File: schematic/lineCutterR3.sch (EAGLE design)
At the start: 63 parts, among them J1 10118192-0001LF, Q1 AO4576, Q2 AO4576, Q4 AO4576, Q5 DMG2305, SW1 KMR2, U1 MS560702BA03-50, U2 MDBT50Q, U3 S25FL128SDPMFIG13S03016, U4 ACS711KEXLT-31AB-T, U6 ICM-20602, X1 2x5 0.05"

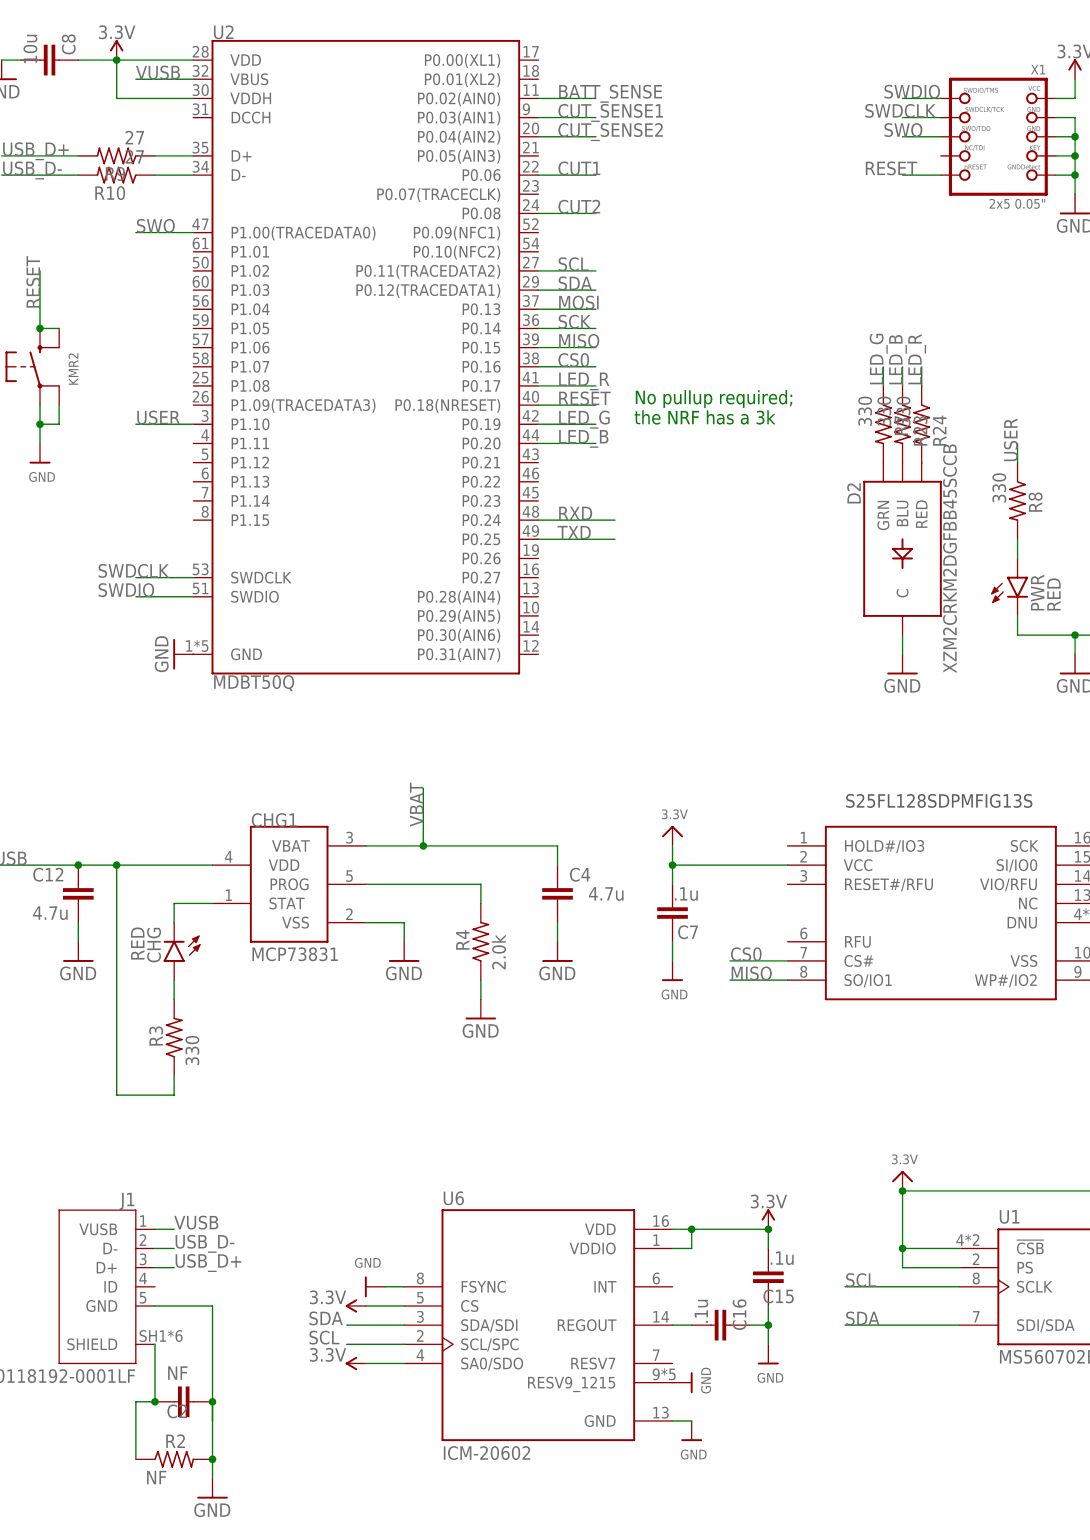
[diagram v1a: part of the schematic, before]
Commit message: R3 PCB: Place most of the components
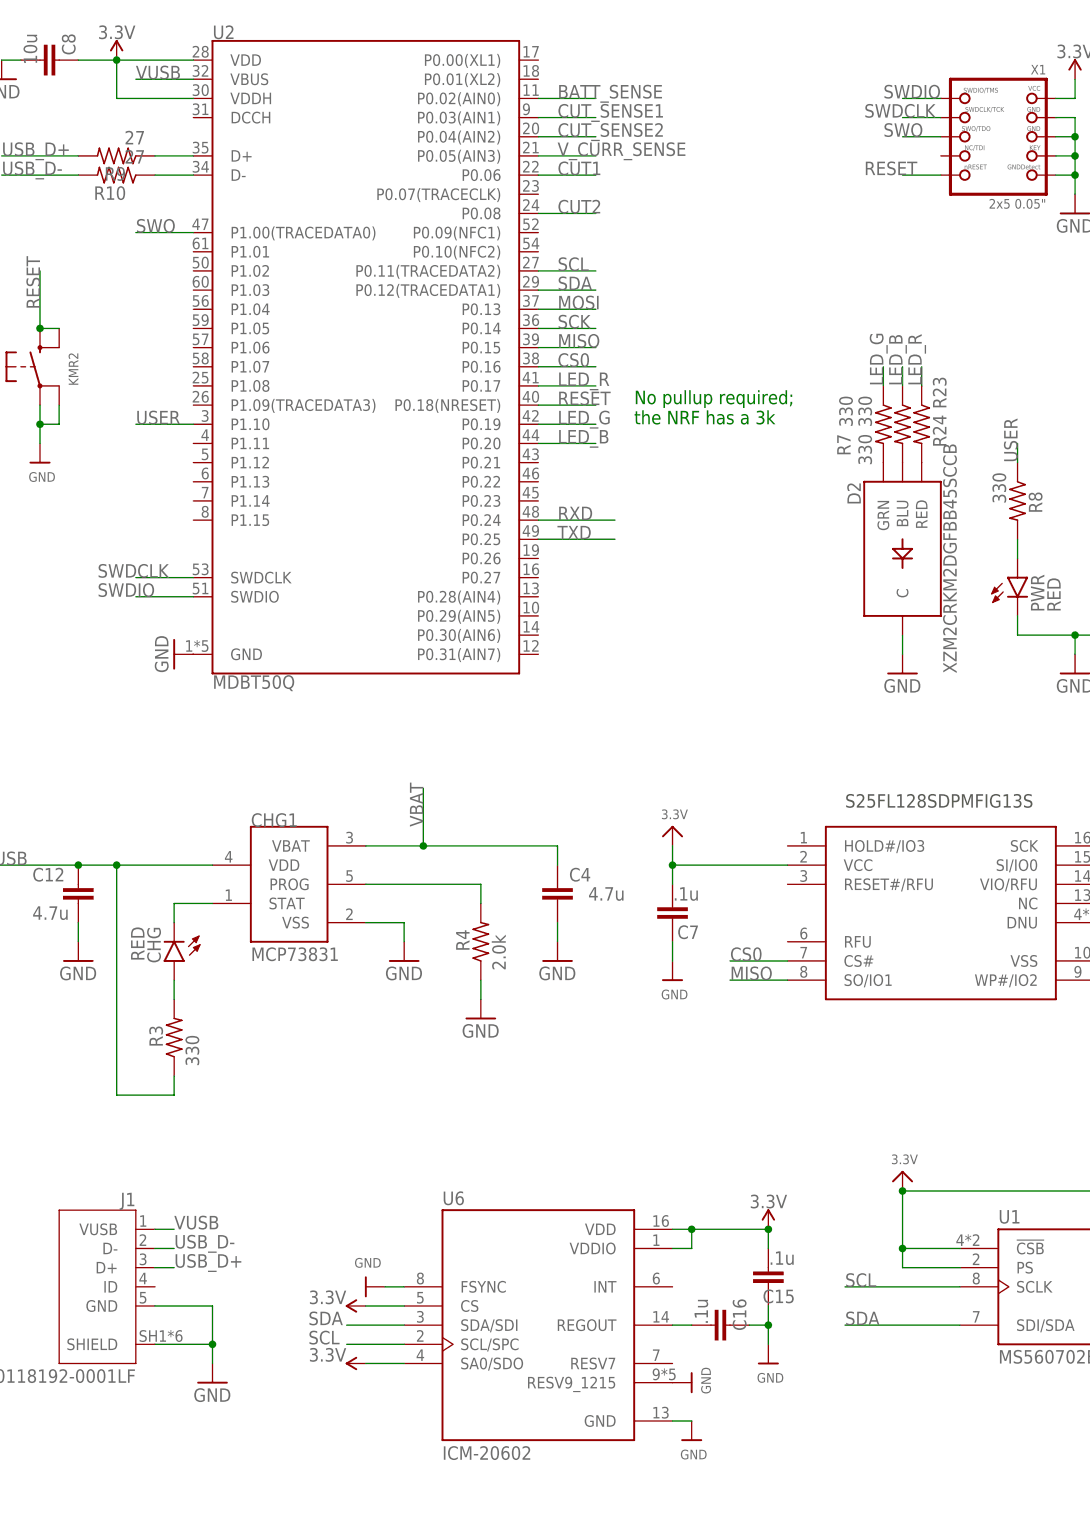
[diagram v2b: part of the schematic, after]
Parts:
- removed C2: NF, rcl:C-EUC0805
- removed R2: NF, rcl:R-US_R0805
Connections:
- removed net N$2: C2.2, J1.SHIELD, R2.1
- net GND: now also J1.SHIELD; no longer C2.1, R2.2
- net V_CURR_SENSE: now also U2.P0.05(AIN3)
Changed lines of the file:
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@@
 <part name="GND12" library="supply1" library_urn="urn:adsk.eagle:library:371" deviceset="GND" device=""/>
 <part name="J1" library="Line Cutter COTS" deviceset="10118192-0001LF" device=""/>
-<part name="C2" library="rcl" library_urn="urn:adsk.eagle:library:334" deviceset="C-EU" device="C0805" package3d_urn="urn:adsk.eagle:package:23617/2" value="NF"/>
-<part name="R2" library="rcl" library_urn="urn:adsk.eagle:library:334" deviceset="R-US_" device="R0805" package3d_urn="urn:adsk.eagle:package:23553/2" value="NF"/>
 <part name="GND1" library="supply1" library_urn="urn:adsk.eagle:library:371" deviceset="GND" device=""/>
 <part name="U1" library="Line Cutter COTS" deviceset="MS560702BA03-50" device=""/>
@@
 <attribute name="VALUE" x="22.868209375" y="20.2995" size="1.78086875" layer="96" rot="MR0"/>
 </instance>
-<instance part="C2" gate="G$1" x="30.48" y="17.78" smashed="yes" rot="R270" grouprefs="CONN_USB">
-<attribute name="NAME" x="26.924" y="15.621" size="1.778" layer="95"/>
-<attribute name="VALUE" x="26.924" y="20.701" size="1.778" layer="96"/>
-</instance>
-<instance part="R2" gate="G$1" x="27.94" y="10.16" smashed="yes" grouprefs="CONN_USB">
-<attribute name="NAME" x="26.67" y="11.6586" size="1.778" layer="95"/>
-<attribute name="VALUE" x="24.13" y="6.858" size="1.778" layer="96"/>
-</instance>
-<instance part="GND1" gate="1" x="33.02" y="5.08" smashed="yes" grouprefs="CONN_USB">
-<attribute name="VALUE" x="30.48" y="2.54" size="1.778" layer="96"/>
+<instance part="GND1" gate="1" x="33.02" y="20.32" smashed="yes" grouprefs="CONN_USB">
+<attribute name="VALUE" x="30.48" y="17.78" size="1.778" layer="96"/>
 </instance>
 <instance part="U1" gate="G$1" x="147.32" y="33.02" smashed="yes" grouprefs="BAROMETER">
@@
 </instance>
 <instance part="R7" gate="G$1" x="121.92" y="147.32" smashed="yes" rot="R270" grouprefs="LEDS">
-<attribute name="NAME" x="123.4186" y="148.59" size="1.778" layer="95" rot="R270"/>
+<attribute name="NAME" x="115.7986" y="146.05" size="1.778" layer="95" rot="R270"/>
 <attribute name="VALUE" x="118.618" y="151.13" size="1.778" layer="96" rot="R270"/>
 </instance>
 <instance part="R23" gate="G$1" x="124.46" y="147.32" smashed="yes" rot="R270" grouprefs="LEDS">
-<attribute name="NAME" x="125.9586" y="148.59" size="1.778" layer="95" rot="R270"/>
-<attribute name="VALUE" x="121.158" y="151.13" size="1.778" layer="96" rot="R270"/>
+<attribute name="NAME" x="128.4986" y="153.67" size="1.778" layer="95" rot="R270"/>
+<attribute name="VALUE" x="118.618" y="146.05" size="1.778" layer="96" rot="R270"/>
 </instance>
 <instance part="R24" gate="G$1" x="127" y="147.32" smashed="yes" rot="R270" grouprefs="LEDS">
 <attribute name="NAME" x="128.4986" y="148.59" size="1.778" layer="95" rot="R270"/>
-<attribute name="VALUE" x="123.698" y="151.13" size="1.778" layer="96" rot="R270"/>
+<attribute name="VALUE" x="116.078" y="151.13" size="1.778" layer="96" rot="R270"/>
 </instance>
 </instances>
@@
 <wire x1="208.28" y1="20.32" x2="208.28" y2="15.24" width="0.1524" layer="91" grouprefs="FETS"/>
 <pinref part="Q1" gate="G$1" pin="S"/>
-</segment>
-<segment>
-<wire x1="33.02" y1="7.62" x2="33.02" y2="10.16" width="0.1524" layer="91" grouprefs="CONN_USB"/>
-<wire x1="33.02" y1="10.16" x2="33.02" y2="17.78" width="0.1524" layer="91" grouprefs="CONN_USB"/>
-<wire x1="33.02" y1="17.78" x2="33.02" y2="15.24" width="0.1524" layer="91" grouprefs="CONN_USB"/>
-<junction x="33.02" y="17.78" grouprefs="CONN_USB"/>
-<junction x="33.02" y="10.16" grouprefs="CONN_USB"/>
-<pinref part="C2" gate="G$1" pin="1"/>
-<pinref part="R2" gate="G$1" pin="2"/>
-<pinref part="GND1" gate="1" pin="GND"/>
-<wire x1="33.02" y1="17.78" x2="33.02" y2="30.48" width="0.1524" layer="91" grouprefs="CONN_USB"/>
-<pinref part="J1" gate="G$1" pin="GND"/>
-<wire x1="33.02" y1="30.48" x2="25.4" y2="30.48" width="0.1524" layer="91" grouprefs="CONN_USB"/>
 </segment>
 <segment>
@@
 <pinref part="R22" gate="G$1" pin="1"/>
 </segment>
+<segment>
+<pinref part="J1" gate="G$1" pin="GND"/>
+<wire x1="33.02" y1="25.4" x2="33.02" y2="30.48" width="0.1524" layer="91" grouprefs="CONN_USB"/>
+<wire x1="33.02" y1="30.48" x2="25.4" y2="30.48" width="0.1524" layer="91" grouprefs="CONN_USB"/>
+<pinref part="J1" gate="G$1" pin="SHIELD"/>
+<wire x1="25.4" y1="25.4" x2="33.02" y2="25.4" width="0.1524" layer="91"/>
+<pinref part="GND1" gate="1" pin="GND"/>
+<wire x1="33.02" y1="25.4" x2="33.02" y2="22.86" width="0.1524" layer="91"/>
+<junction x="33.02" y="25.4"/>
+</segment>
 </net>
 <net name="VUSB" class="0">
@@
 </segment>
 </net>
-<net name="N$2" class="0">
-<segment>
-<wire x1="22.86" y1="10.16" x2="22.86" y2="17.78" width="0.1524" layer="91" grouprefs="CONN_USB"/>
-<wire x1="22.86" y1="17.78" x2="25.4" y2="17.78" width="0.1524" layer="91" grouprefs="CONN_USB"/>
-<wire x1="25.4" y1="25.4" x2="25.4" y2="17.78" width="0.1524" layer="91" grouprefs="CONN_USB"/>
-<junction x="25.4" y="17.78" grouprefs="CONN_USB"/>
-<pinref part="J1" gate="G$1" pin="SHIELD"/>
-<pinref part="C2" gate="G$1" pin="2"/>
-<pinref part="R2" gate="G$1" pin="1"/>
-</segment>
-</net>
 <net name="SCK" class="0">
 <segment>
@@
 <label x="254" y="78.74" size="1.778" layer="95" grouprefs="BATTERY"/>
 </segment>
-</net>
+<segment>
+<pinref part="U2" gate="G$1" pin="P0.05(AIN3)"/>
+<wire x1="76.2" y1="182.88" x2="83.82" y2="182.88" width="0.1524" layer="91"/>
+<label x="78.74" y="182.88" size="1.778" layer="95"/>
+</segment>
+</net>

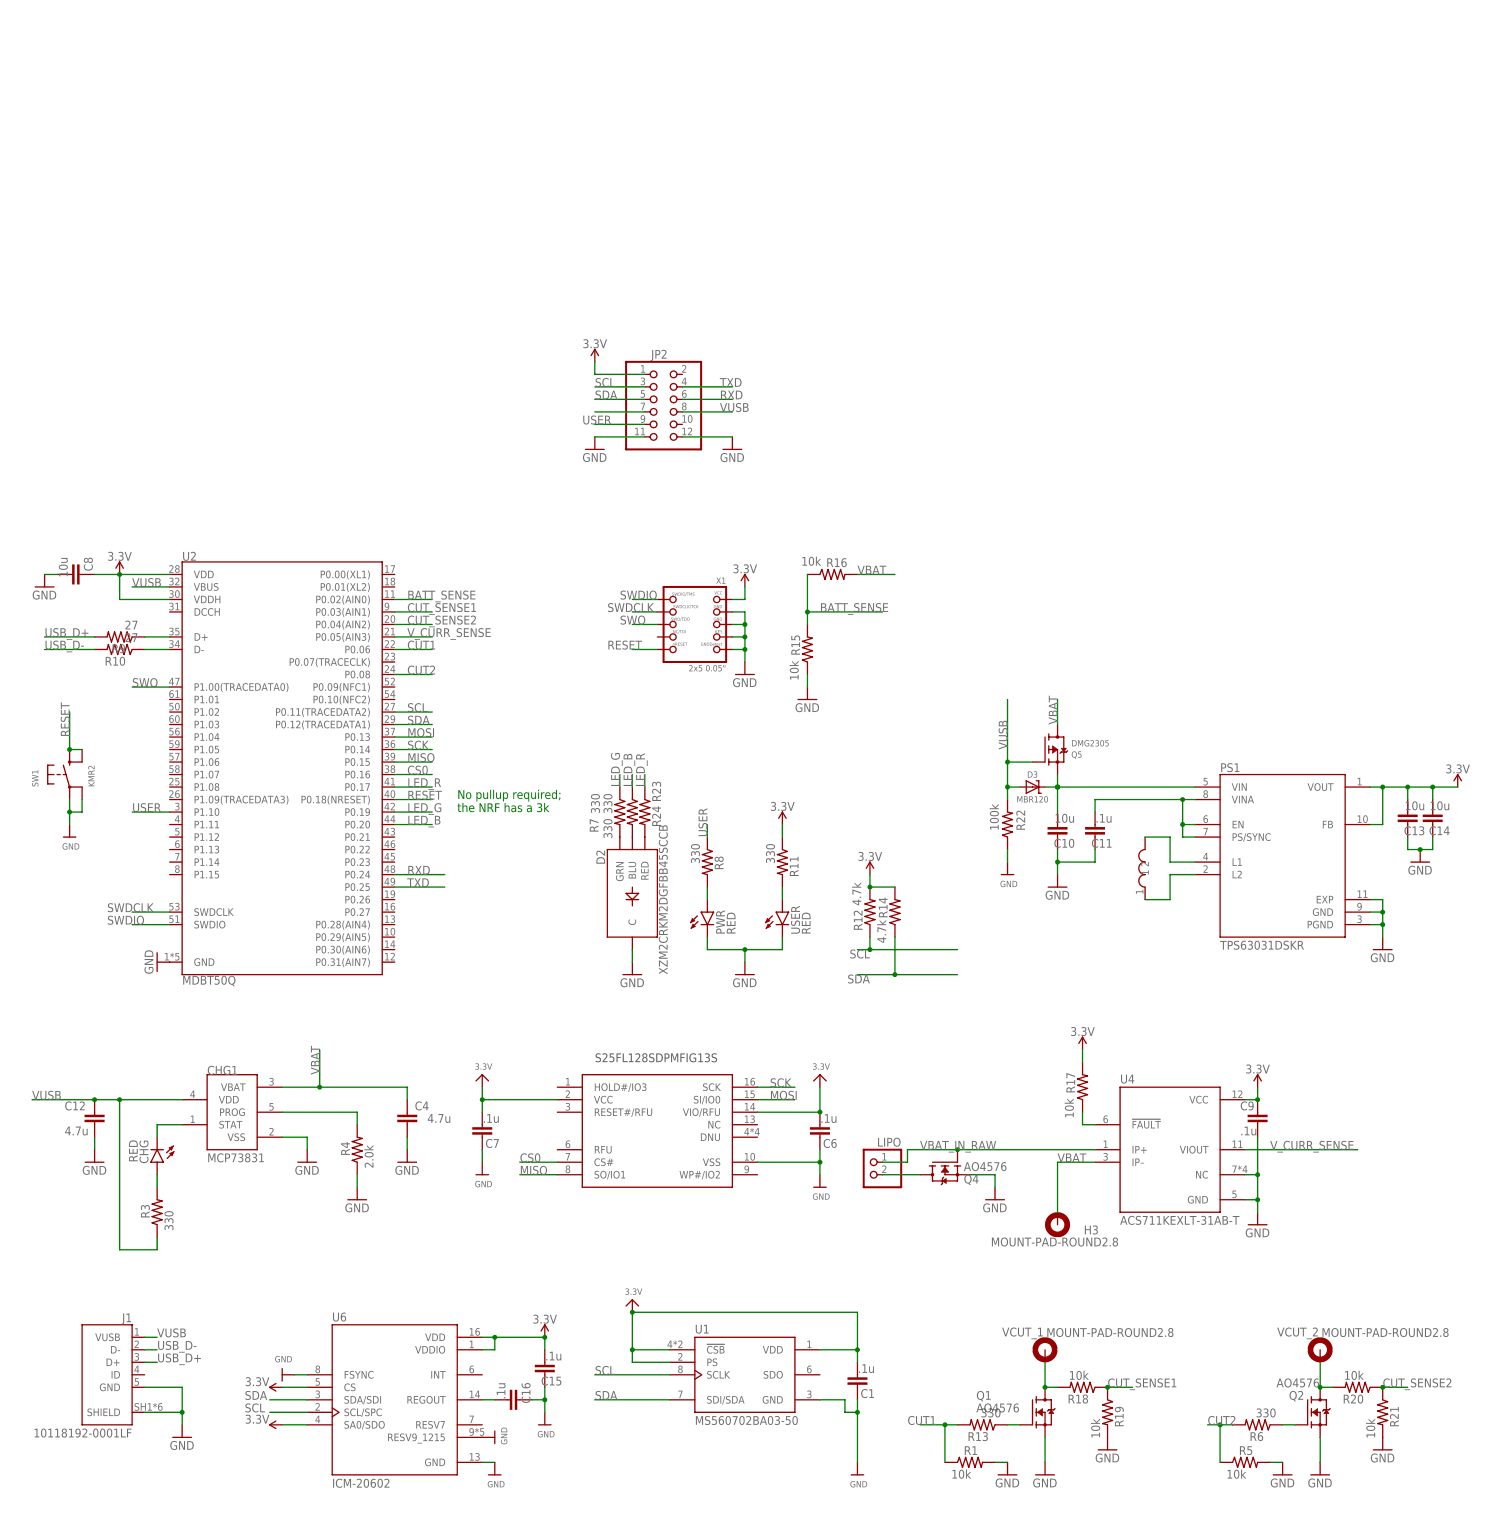
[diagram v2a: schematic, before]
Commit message: Pass 1 at routing line cutter R3
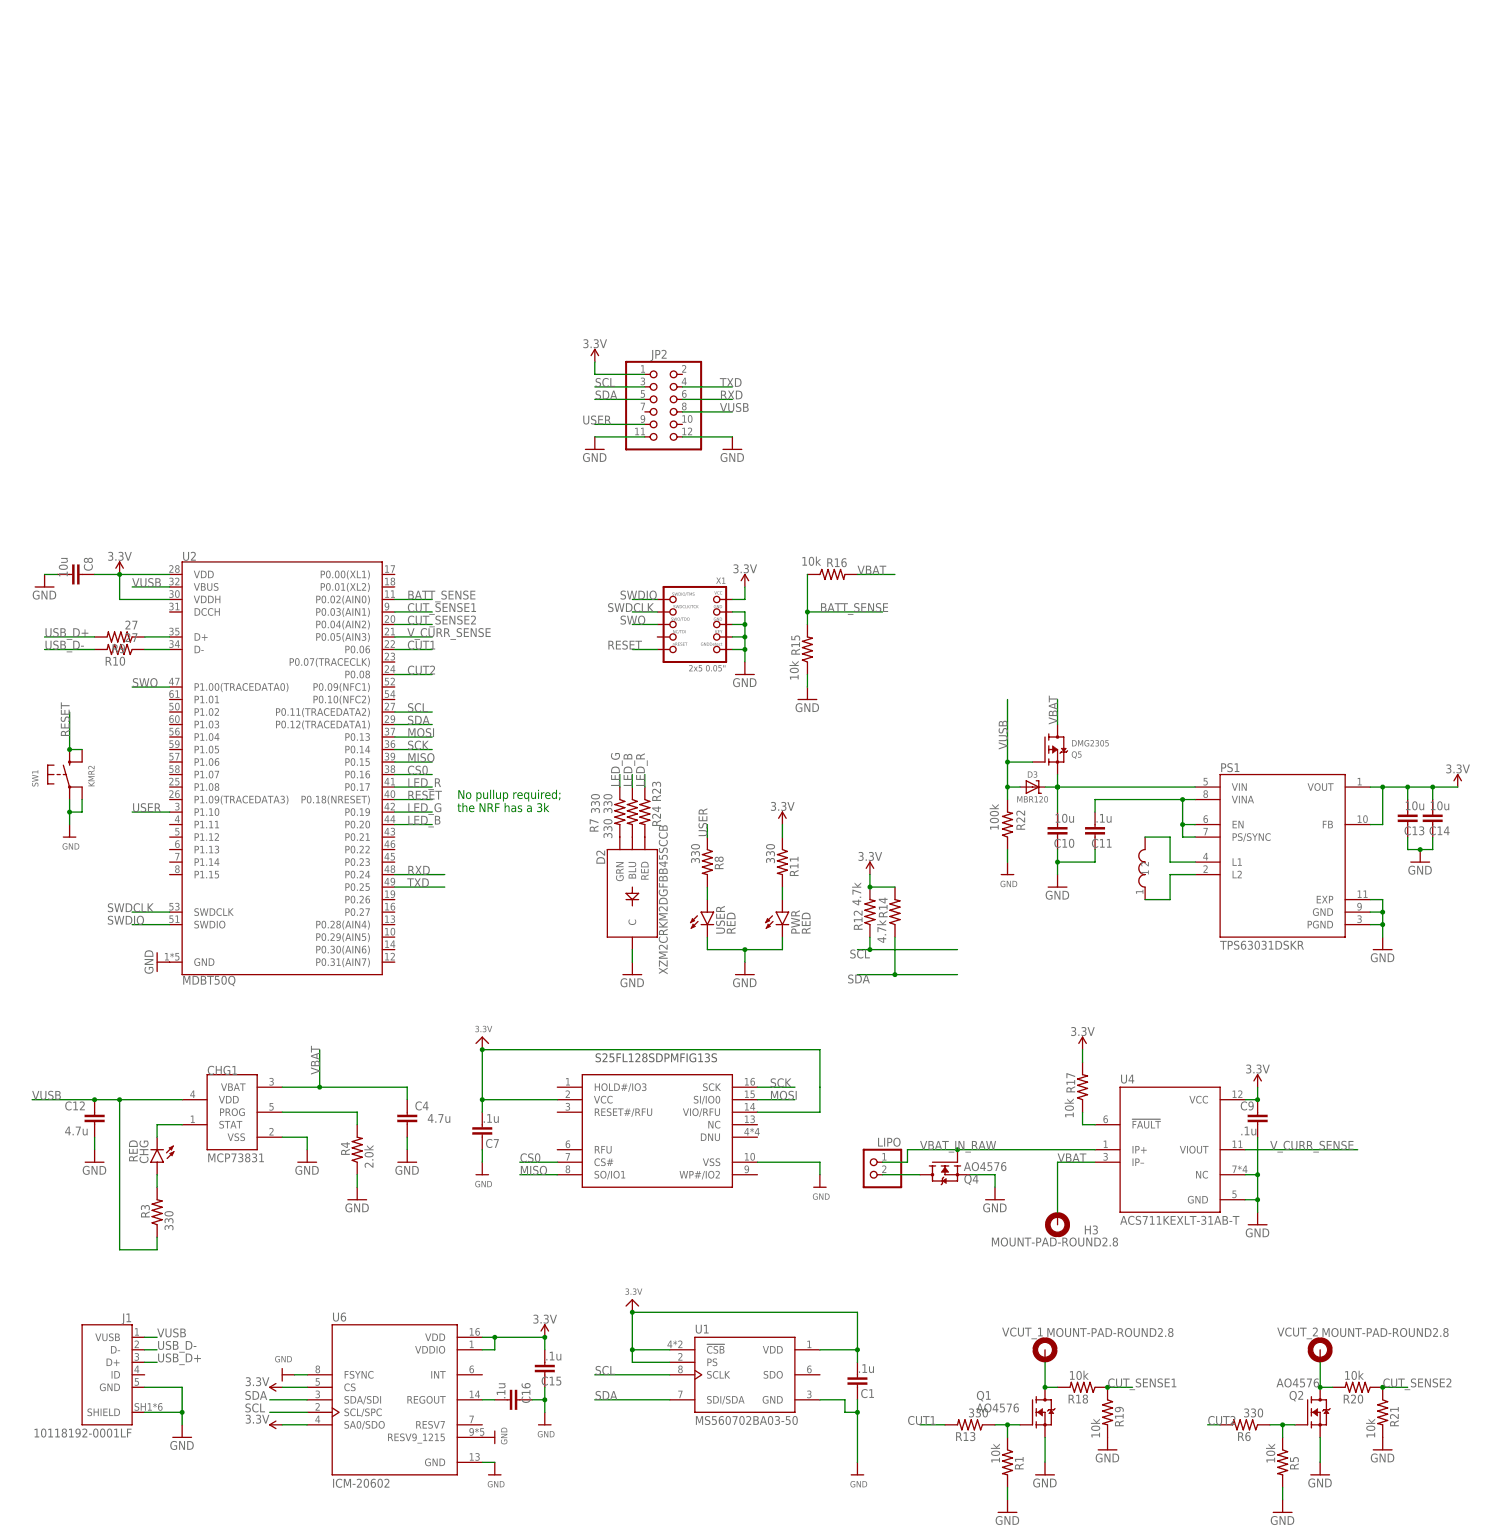
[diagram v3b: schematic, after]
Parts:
- removed C6: .1u, rcl:C-EUC0805
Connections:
- removed net N$13: JP2.7
- net 3.3V: no longer C6.2
- net CUT1: no longer R1.1
- net CUT2: no longer R5.1
- net GND: no longer C6.1
- net N$10: now also R1.1
- net N$3: now also R5.1
- net N$7: now also USER.A; no longer PWR.A
- net N$9: now also PWR.A; no longer USER.A
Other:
- moved on the sheet: PWR, R1, R13, R5, R6, USER
